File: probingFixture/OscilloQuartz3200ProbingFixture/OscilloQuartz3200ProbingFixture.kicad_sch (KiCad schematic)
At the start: 5 parts, among them J1 DB25_Plug

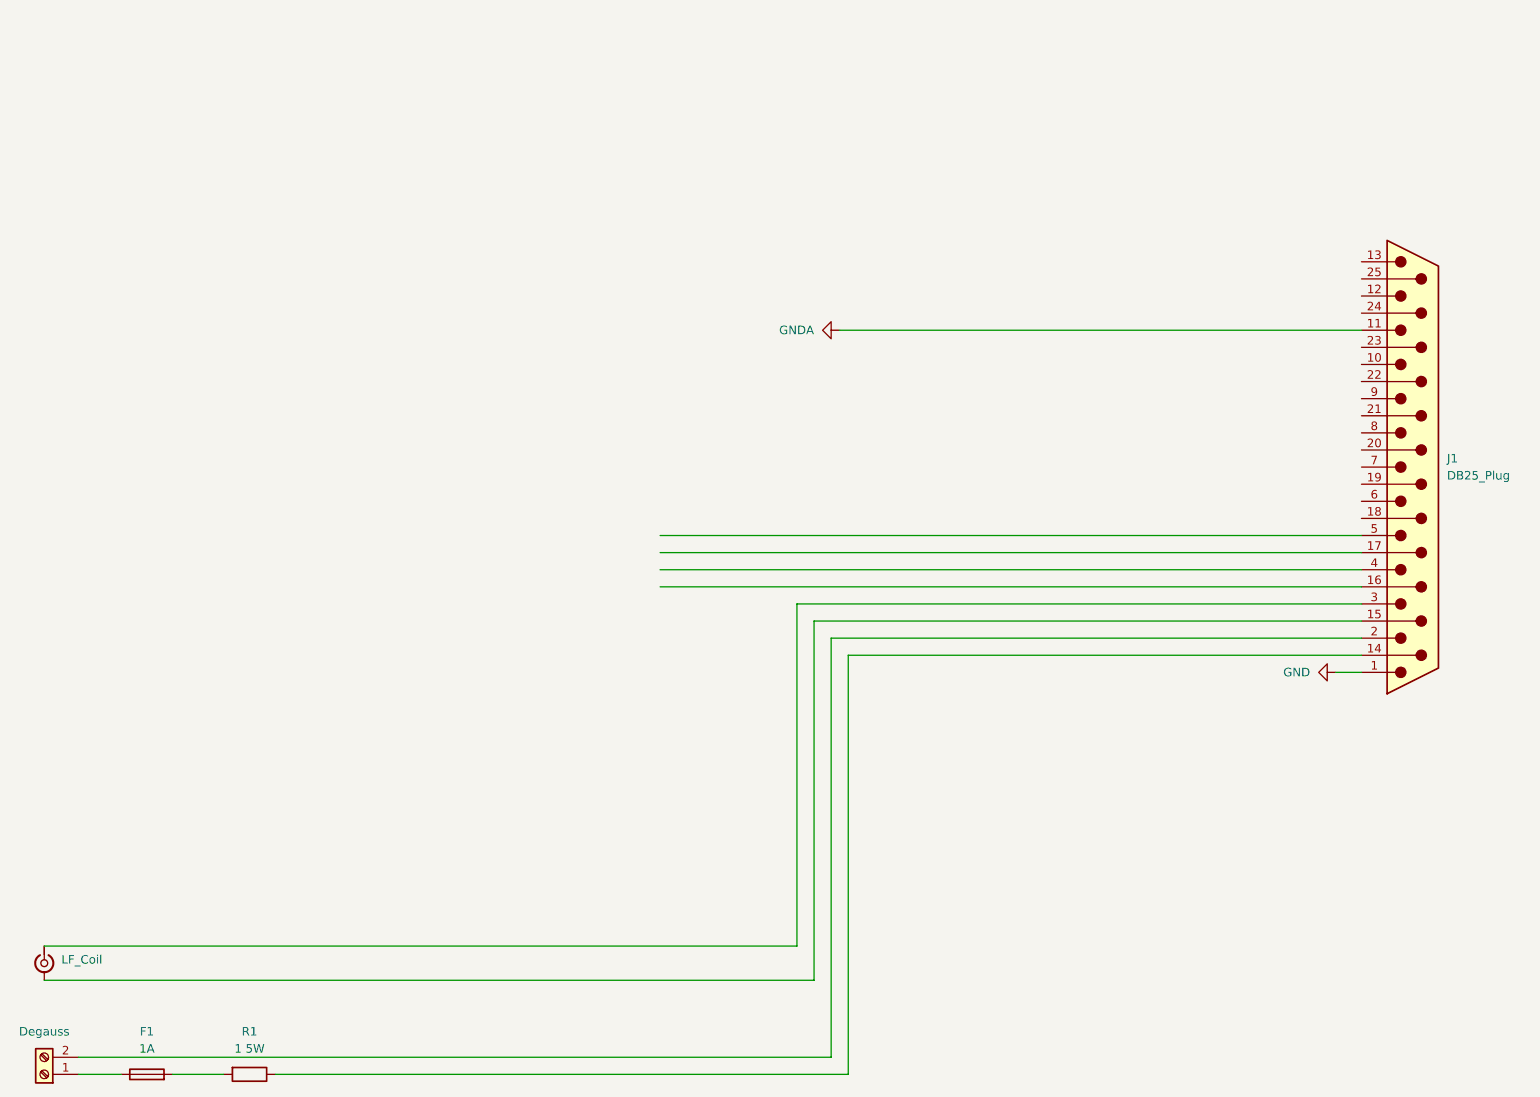
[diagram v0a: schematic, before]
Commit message: Added TIA for pump current
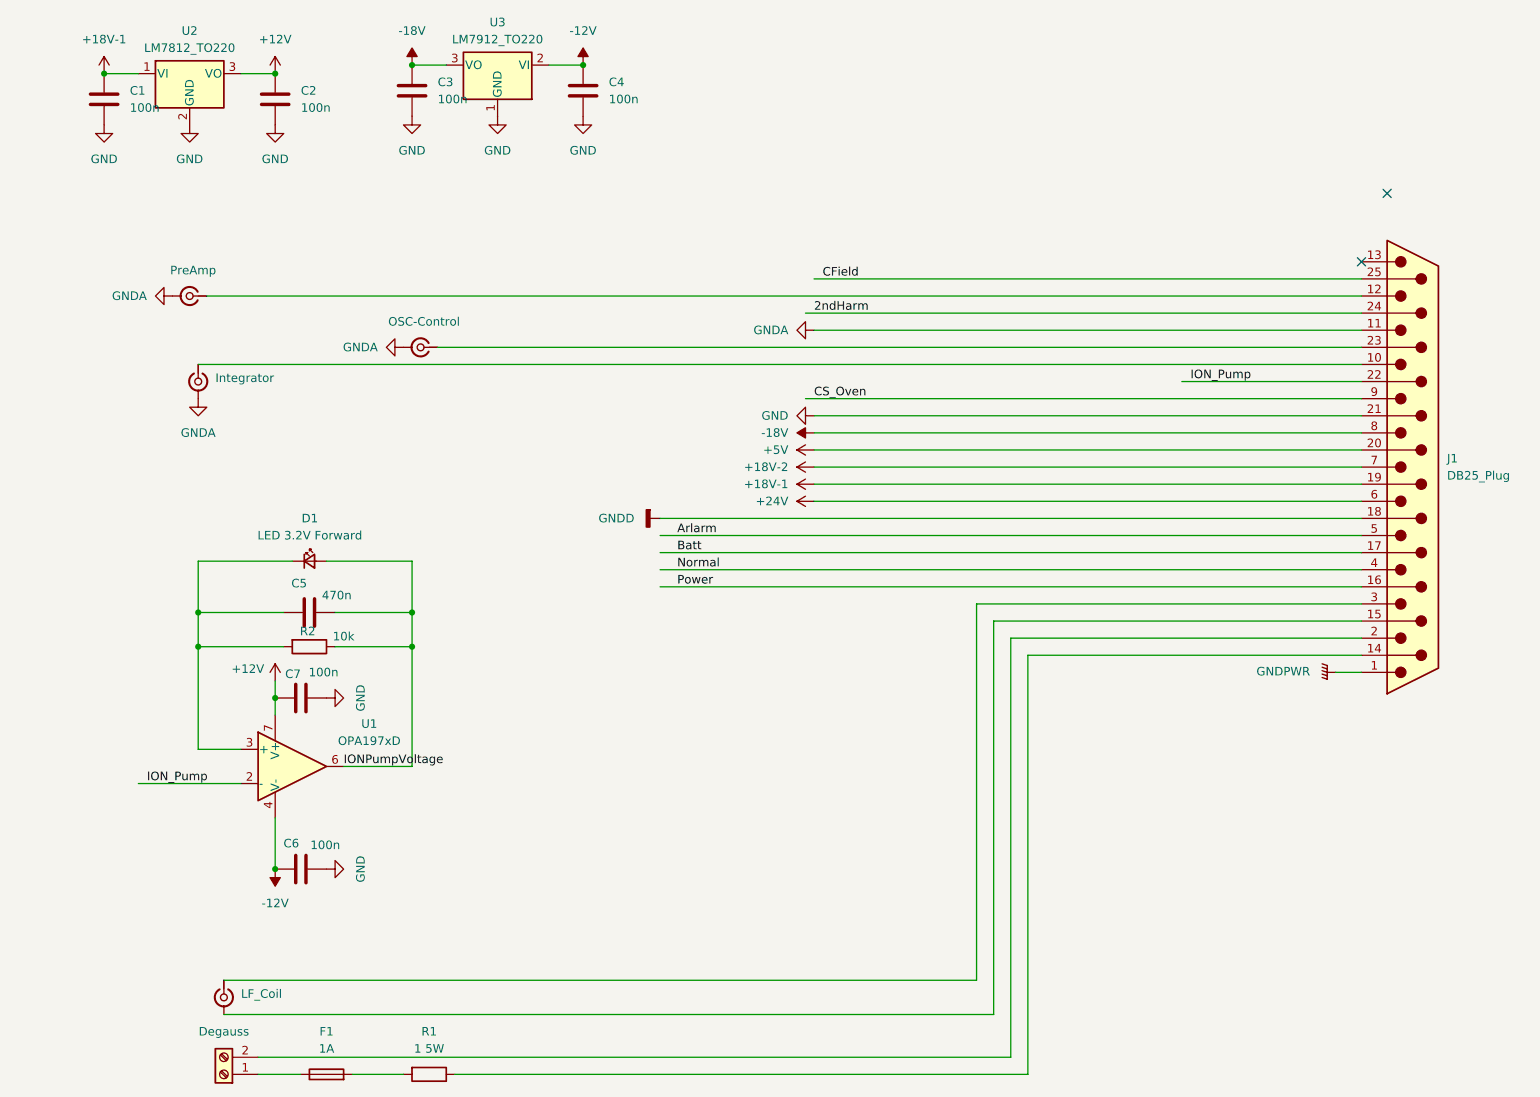
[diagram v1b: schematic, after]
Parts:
- added C1, C2, C3, C4, C6, C7: 100n, Capacitor_SMD:C_0805_2012Metric_Pad1.18x1.45mm_HandSolder, symbol Device:C
- added C5: 470n, Capacitor_SMD:C_0805_2012Metric_Pad1.18x1.45mm_HandSolder, symbol Device:C
- added D1: LED 3.2V Forward, LED_THT:LED_D3.0mm_Clear, symbol Device:LED_Small
- added Integrator, OSC-Control, PreAmp: Conn_Coaxial_Small, Connector_Coaxial:SMA_Amphenol_901-143_Horizontal, symbol Connector:Conn_Coaxial_Small
- added R2: 10k, Resistor_SMD:R_0805_2012Metric, symbol Device:R
- added U1: OPA197xD, Package_SO:SOIC-8_3.9x4.9mm_P1.27mm, symbol Amplifier_Operational:OPA197xD
- added U2: LM7812_TO220, Package_TO_SOT_THT:TO-220-3_Vertical, symbol Regulator_Linear:LM7812_TO220
- added U3: LM7912_TO220, Package_TO_SOT_THT:TO-220-3_Vertical, symbol Regulator_Linear:LM7912_TO220
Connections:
- net GND: now also J1.21 (P21), C1.2, C2.2, C3.2, C4.2, C6.2, C7.2, U2.2 (GND), U3.1 (GND); no longer J1.1
- net GNDA: now also Integrator.2 (Ext), OSC-Control.2 (Ext), PreAmp.2 (Ext)
- net at J1.10: now also Integrator.1 (In)
- net at J1.12: now also PreAmp.1 (In)
- net Power: now reaches J1.16 (P16)
- net Batt: now reaches J1.17 (P17)
- net GNDD: now reaches J1.18 (P18)
- net +18V-1: now reaches J1.19 (P19)
- net +18V-1: now also C1.1, U2.1 (VI)
- net +5V: now reaches J1.20 (P20)
- net ION_Pump: now reaches J1.22 (P22)
- net ION_Pump: now also U1.2 (-)
- net at J1.23 (P23): now also OSC-Control.1 (In)
- net 2ndHarm: now reaches J1.24 (P24)
- net CField: now reaches J1.25 (P25)
- net Normal: now reaches J1.4
- net Arlarm: now reaches J1.5
- net +24V: now reaches J1.6
- net +18V-2: now reaches J1.7
- net -18V: now reaches J1.8
- net -18V: now also C3.1, U3.3 (VO)
- net CS_Oven: now reaches J1.9
- new net: C5.1, D1.1 (K), R2.2, U1.3 (+)
- new net +12V: C2.1, C7.1, U1.7 (V+), U2.3 (VO)
- new net -12V: C4.1, C6.1, U1.4 (V-), U3.2 (VI)
- new net GNDPWR: J1.1
- new net IONPumpVoltage: C5.2, D1.2 (A), R2.1, U1.6
- no-connect marks 0 -> 2
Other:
- moved on the sheet: Degauss, F1, LF_Coil, R1
